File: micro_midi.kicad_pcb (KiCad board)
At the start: 2 copper layers, 67 parts, among them U1 74HC595, U2 Arduino_Micro, U3 74HC595

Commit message: resistor change and pdf
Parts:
- R1, R10, R11, R12, R13, R14, R15, R16, R2, R3, R4, R5, R6, R7, R8, R9: footprint ScottoKeebs_Components:Resistor_0402 -> Resistor_THT:R_Axial_DIN0204_L3.6mm_D1.6mm_P1.90mm_Vertical

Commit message: nearing completion
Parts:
- removed R10, R11, R12, R13, R14, R15, R16, R4, R5, R6, R7, R8, R9: Resistor, Resistor_THT:R_Axial_DIN0204_L3.6mm_D1.6mm_P1.90mm_Vertical
- removed U1, U3: 74HC595, Package_SO:SSOP-16_5.3x6.2mm_P0.65mm
- removed U2: Arduino_Micro, Arduino:Arduino_Micro
- added C0: MountingHole_Pad, TestPoint:TestPoint_Plated_Hole_D3.0mm, F.Cu at (49.8, 49.8)
- added C1: MountingHole_Pad, TestPoint:TestPoint_Plated_Hole_D3.0mm, F.Cu at (57.0, 49.8)
- added C2: MountingHole_Pad, TestPoint:TestPoint_Plated_Hole_D3.0mm, F.Cu at (64.1, 49.8)
- added C3: MountingHole_Pad, TestPoint:TestPoint_Plated_Hole_D3.0mm, F.Cu at (71.2, 49.8)
- added GND1: MountingHole_Pad, TestPoint:TestPoint_Plated_Hole_D3.0mm, F.Cu at (142.4, 49.8)
- added L0: MountingHole_Pad, TestPoint:TestPoint_Plated_Hole_D3.0mm, F.Cu at (85.4, 49.8)
- added L1: MountingHole_Pad, TestPoint:TestPoint_Plated_Hole_D3.0mm, F.Cu at (89.0, 54.9)
- added L10: MountingHole_Pad, TestPoint:TestPoint_Plated_Hole_D3.0mm, F.Cu at (121.0, 49.8)
- added L11: MountingHole_Pad, TestPoint:TestPoint_Plated_Hole_D3.0mm, F.Cu at (124.6, 54.9)
- added L12: MountingHole_Pad, TestPoint:TestPoint_Plated_Hole_D3.0mm, F.Cu at (128.2, 49.8)
- added L13: MountingHole_Pad, TestPoint:TestPoint_Plated_Hole_D3.0mm, F.Cu at (131.7, 54.9)
- added L14: MountingHole_Pad, TestPoint:TestPoint_Plated_Hole_D3.0mm, F.Cu at (135.3, 49.8)
- added L15: MountingHole_Pad, TestPoint:TestPoint_Plated_Hole_D3.0mm, F.Cu at (138.8, 54.9)
- added L2: MountingHole_Pad, TestPoint:TestPoint_Plated_Hole_D3.0mm, F.Cu at (92.6, 49.8)
- added L3: MountingHole_Pad, TestPoint:TestPoint_Plated_Hole_D3.0mm, F.Cu at (96.1, 54.9)
- added L4: MountingHole_Pad, TestPoint:TestPoint_Plated_Hole_D3.0mm, F.Cu at (99.7, 49.8)
- added L5: MountingHole_Pad, TestPoint:TestPoint_Plated_Hole_D3.0mm, F.Cu at (103.2, 54.9)
- added L6: MountingHole_Pad, TestPoint:TestPoint_Plated_Hole_D3.0mm, F.Cu at (106.8, 49.8)
- added L7: MountingHole_Pad, TestPoint:TestPoint_Plated_Hole_D3.0mm, F.Cu at (110.4, 54.9)
- added L8: MountingHole_Pad, TestPoint:TestPoint_Plated_Hole_D3.0mm, F.Cu at (113.9, 49.8)
- added L9: MountingHole_Pad, TestPoint:TestPoint_Plated_Hole_D3.0mm, F.Cu at (117.5, 54.9)
- added R0: MountingHole_Pad, TestPoint:TestPoint_Plated_Hole_D3.0mm, F.Cu at (53.4, 54.9)
- R1, R2, R3: value Resistor -> MountingHole_Pad; footprint Resistor_THT:R_Axial_DIN0204_L3.6mm_D1.6mm_P1.90mm_Vertical -> TestPoint:TestPoint_Plated_Hole_D3.0mm
- moved R1 63.6 mm to (60.5, 54.9), turned to 0 degrees
- moved D25 59.8 mm to (45.8, 101.2)
- moved S1 59.8 mm to (47.0, 72.3)
- moved S9 59.8 mm to (47.0, 96.1)
- moved D1 59.8 mm to (56.6, 76.2)
- moved D17 59.8 mm to (45.8, 77.4)
- moved D9 59.8 mm to (56.6, 100.0)
- moved R2 54.1 mm to (67.6, 54.9), turned to 0 degrees
- moved D26 53.3 mm to (74.3, 101.2)
- moved D18 53.3 mm to (74.3, 77.4)
- moved S10 53.3 mm to (75.6, 96.1)
- moved S2 53.3 mm to (75.6, 72.3)
- moved D10 53.3 mm to (85.1, 100.0)
- moved D2 53.3 mm to (85.1, 76.2)
- moved R3 50.9 mm to (74.8, 54.9), turned to 0 degrees
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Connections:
- net /COL 0 renamed Net-(C0-Pad1)
- net /COL 1 renamed Net-(C1-Pad1)
- net /COL 2 renamed Net-(C2-Pad1)
- net /COL 3 renamed Net-(C3-Pad1)
- net /ROW 0 renamed Net-(D1-K)
- net GND renamed Net-(D17-K)
- D10 pad 1: /ROW 1 -> Net-(D10-K)
- D11 pad 1: /ROW 1 -> Net-(D10-K)
- D12 pad 1: /ROW 1 -> Net-(D10-K)
- D13 pad 1: /ROW 3 -> Net-(D13-K)
- D14 pad 1: /ROW 3 -> Net-(D13-K)
- D15 pad 1: /ROW 3 -> Net-(D13-K)
- D16 pad 1: /ROW 3 -> Net-(D13-K)
- D5 pad 1: /ROW 2 -> Net-(D5-K)
- D6 pad 1: /ROW 2 -> Net-(D5-K)
- D7 pad 1: /ROW 2 -> Net-(D5-K)
- D8 pad 1: /ROW 2 -> Net-(D5-K)
- D9 pad 1: /ROW 1 -> Net-(D10-K)
- R1 pad 1: Net-(U1-QA) -> Net-(D10-K)
- R2 pad 1: Net-(U1-QB) -> Net-(D5-K)
- R3 pad 1: Net-(U1-QC) -> Net-(D13-K)
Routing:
- net Net-(D17-K): track 0.00 -> 762.9 mm
- net Net-(D13-K): track 0.00 -> 312.8 mm
- net Net-(D5-K): track 0.00 -> 295.1 mm
- net Net-(C3-Pad1): track 0.00 -> 241.5 mm, vias 0 -> 6
- net Net-(C2-Pad1): track 0.00 -> 220.2 mm, vias 0 -> 4
- net Net-(D10-K): track 0.00 -> 211.9 mm
- net Net-(C1-Pad1): track 0.00 -> 203.6 mm, vias 0 -> 2
- net Net-(C0-Pad1): track 0.00 -> 201.2 mm
- net Net-(D32-A): track 0.00 -> 154.7 mm, vias 0 -> 2
- net Net-(D24-A): track 0.00 -> 147.7 mm
- net Net-(D1-K): track 57.2 -> 193.8 mm
- net Net-(D31-A): track 0.00 -> 131.6 mm, vias 0 -> 2
- net Net-(D23-A): track 0.00 -> 127.1 mm
- net Net-(D30-A): track 0.00 -> 99.4 mm, vias 0 -> 2
- net Net-(D25-A): track 0.00 -> 99.2 mm, vias 0 -> 2
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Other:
- board outline added: 231.1 x 65.6 mm

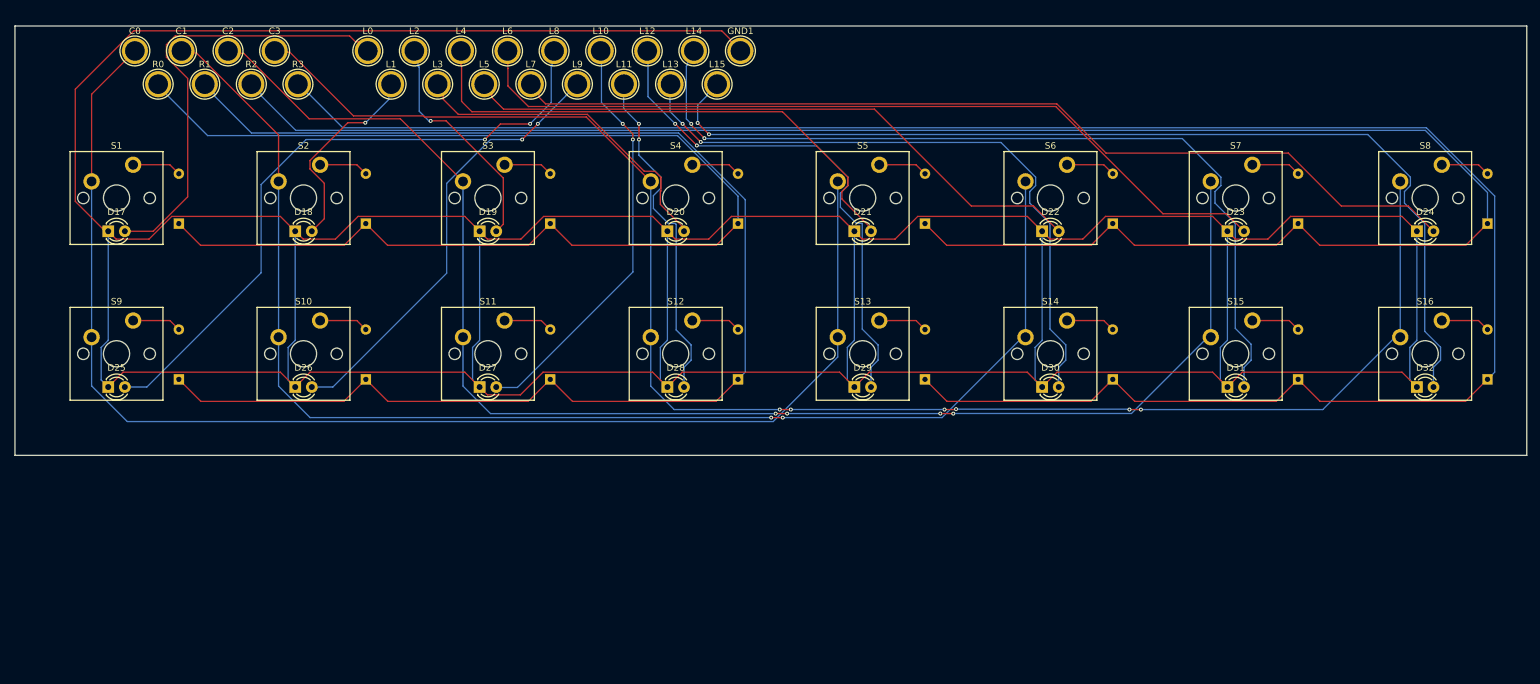
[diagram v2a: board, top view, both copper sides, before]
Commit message: made svg
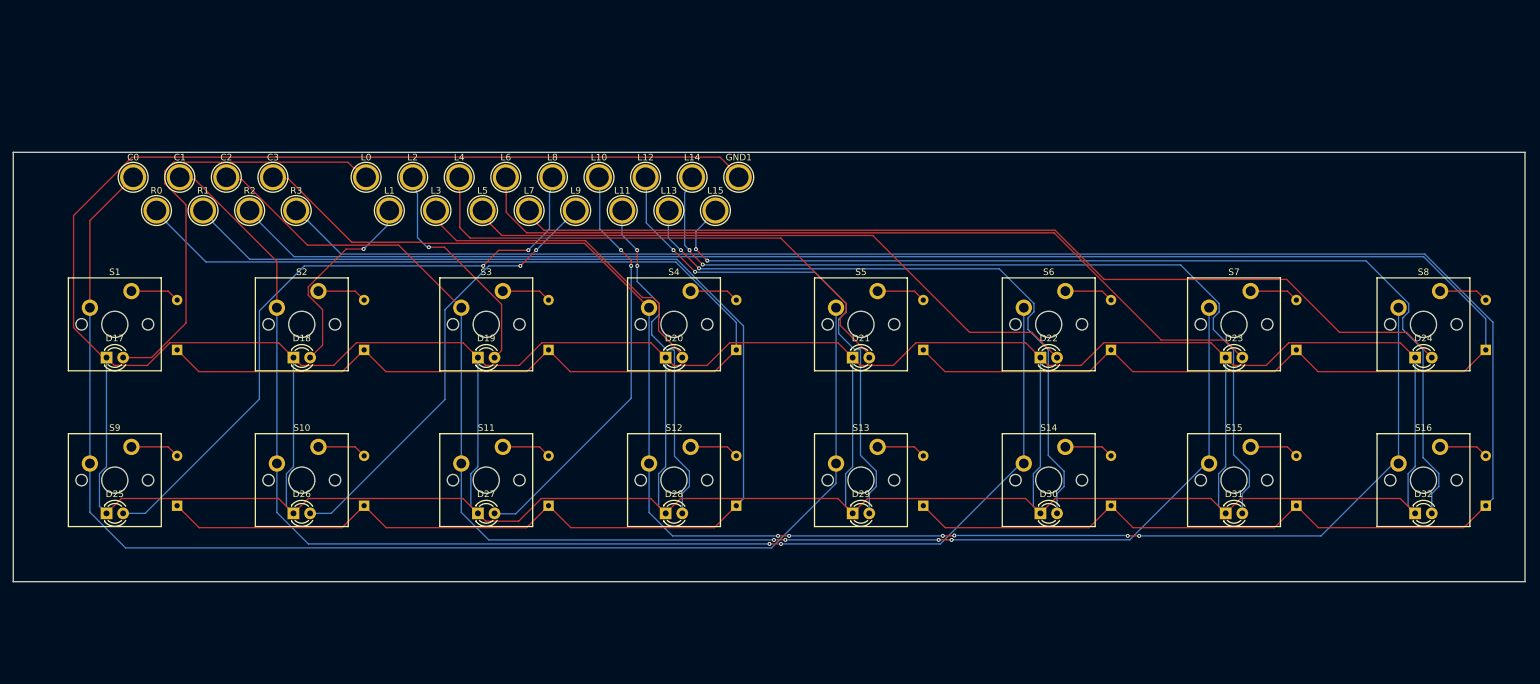
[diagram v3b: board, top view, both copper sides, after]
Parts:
- moved C0 19.3 mm to (49.6, 69.2)
- moved C1 19.3 mm to (56.7, 69.2)
- moved C2 19.3 mm to (63.8, 69.2)
- moved C3 19.3 mm to (70.9, 69.2)
- moved D1 19.3 mm to (56.3, 95.5)
- moved D10 19.3 mm to (84.9, 119.3)
- moved D11 19.3 mm to (113.1, 119.3)
- moved D12 19.3 mm to (141.8, 119.3)
- moved D13 19.3 mm to (170.3, 119.3)
- moved D14 19.3 mm to (199.0, 119.3)
- moved D15 19.3 mm to (227.4, 119.3)
- moved D16 19.3 mm to (256.3, 119.3)
- moved D17 19.3 mm to (45.5, 96.7)
- moved D18 19.3 mm to (74.1, 96.7)
- moved D19 19.3 mm to (102.3, 96.7)
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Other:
- board text added: "04/11/2024"
- board text added: "D. Bruce Cahilly III"
- board text added: "Micro Midi v2 Button Panel"

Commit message: updated screw positions
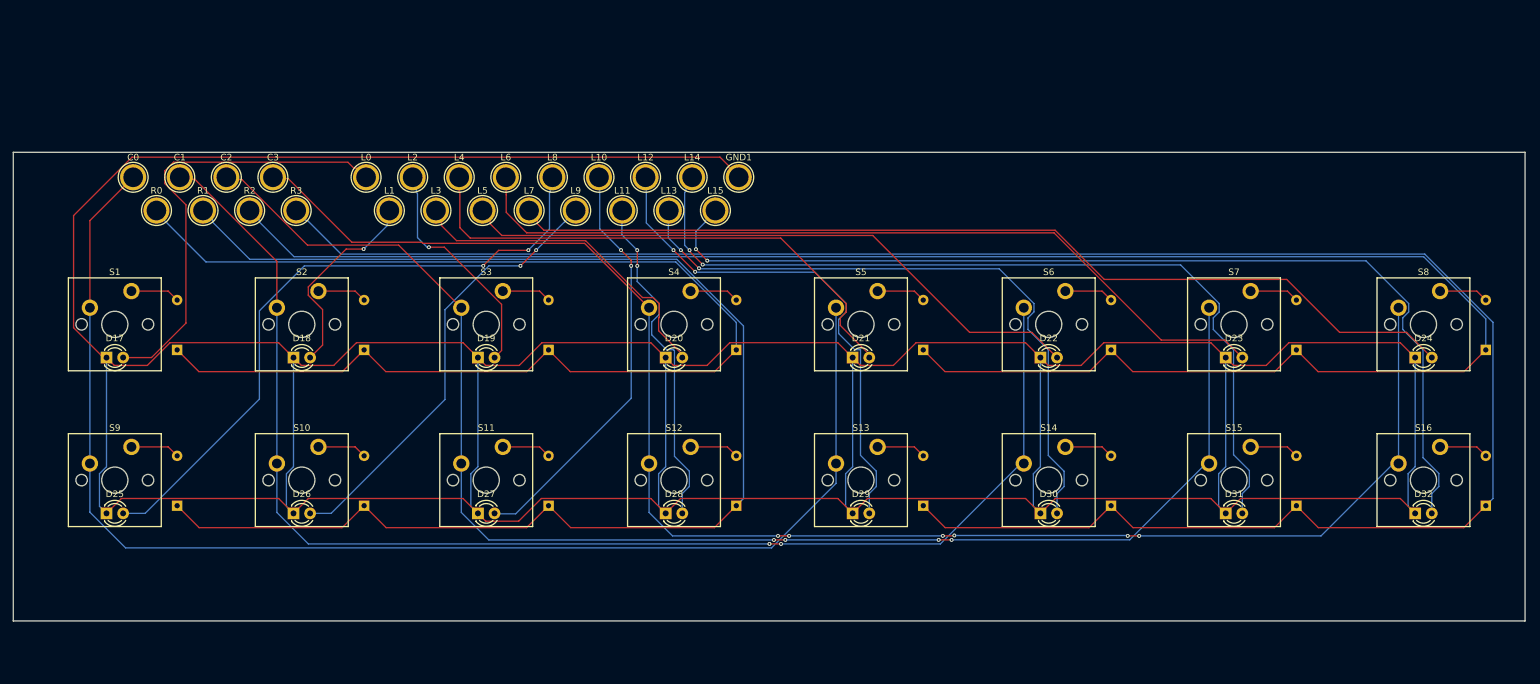
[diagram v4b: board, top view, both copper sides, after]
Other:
- board size 231.1 x 65.6 mm -> 231.1 x 71.6 mm
- board text added: "*"
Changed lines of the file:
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@@
 		(pad_to_mask_clearance 0)
 		(allow_soldermask_bridges_in_footprints no)
-		(grid_origin 31.51 46.024)
+		(grid_origin 262.328076 136.966049)
 		(pcbplotparams
 			(layerselection 0x00010fc_ffffffff)
@@
 			(pdf_back_fp_property_popups yes)
 			(dxfpolygonmode yes)
-			(dxfimperialunits yes)
+			(dxfimperialunits no)
 			(dxfusepcbnewfont yes)
 			(psnegative no)
@@
 			(sketchpadsonfab no)
 			(subtractmaskfromsilk no)
-			(outputformat 1)
+			(outputformat 3)
 			(mirror no)
-			(drillshape 1)
+			(drillshape 0)
 			(scaleselection 1)
-			(outputdirectory "")
+			(outputdirectory "./")
 		)
 	)
@@
 	(gr_rect
 		(start 31.248076 65.334049)
-		(end 262.328076 130.966049)
+		(end 262.328076 136.966049)
 		(stroke
 			(width 0.05)
@@
 		(layer "Edge.Cuts")
 	)
+	(gr_text "*"
+		(at 255.560438 132.366422 0)
+		(layer "F.Fab")
+		(effects
+			(font
+				(size 1.5 1.5)
+				(thickness 0.3)
+				(bold yes)
+			)
+			(justify left bottom)
+		)
+	)
+	(gr_text "*"
+		(at 36.510612 72.643482 0)
+		(layer "F.Fab")
+		(effects
+			(font
+				(size 1.5 1.5)
+				(thickness 0.3)
+				(bold yes)
+			)
+			(justify left bottom)
+		)
+	)
+	(gr_text "*"
+		(at 255.554484 72.674668 0)
+		(layer "F.Fab")
+		(effects
+			(font
+				(size 1.5 1.5)
+				(thickness 0.3)
+				(bold yes)
+			)
+			(justify left bottom)
+		)
+	)
+	(gr_text "*"
+		(at 36.516566 132.335236 0)
+		(layer "F.Fab")
+		(effects
+			(font
+				(size 1.5 1.5)
+				(thickness 0.3)
+				(bold yes)
+			)
+			(justify left bottom)
+		)
+	)
 	(gr_text "04/11/2024"
